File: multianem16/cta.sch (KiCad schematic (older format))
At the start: 243 parts, among them Q1 TIP41, Q10 TIP41, Q11 TIP41, Q12 TIP41, Q13 TIP41, Q14 TIP41, Q15 TIP41, Q16 TIP41, Q2 TIP41, Q3 TIP41, Q4 TIP41, Q5 TIP41, Q6 TIP41, Q7 TIP41, Q8 TIP41, Q9 TIP41, U1 LM324, U10 LM324, U11 LM324, U12 LM324, U13 LM324, U14 LM324, U15 LM324, U16 LM324, U2 LM324, U3 LM324, U4 LM324, U5 LM324, U6 LM324, U7 LM324, U8 LM324, U9 LM324

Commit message: Working on making the multinanem16 board use symmetric power input.
This way I can use more types of op-amps.
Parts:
- removed Cua1, Cua2, Cua3, Cua4, Cua5: 10u, Capacitor_THT:CP_Radial_D5.0mm_P2.50mm, symbol Device:CP
- removed JVIN1: Conn_01x02, TerminalBlock:TerminalBlock_bornier-2_P5.08mm, symbol Connector_Generic:Conn_01x02
- added Cua1, Cua2, Cua3, Cua4, Cua5: 100n, Capacitor_THT:C_Rect_L7.2mm_W3.5mm_P5.00mm_FKS2_FKP2_MKS2_MKP2, symbol Device:C
- added JVIN1: Conn_01x06, TerminalBlock:TerminalBlock_bornier-6_P5.08mm, symbol Connector_Generic:Conn_01x06
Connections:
- net GND: now also Cua1.2, Cua2.2, Cua3.2, Cua4.2, Cua5.2, JVIN1.3 (Pin_3), JVIN1.4 (Pin_4); no longer U1.11 (V-), U2.11 (V-), U3.11 (V-), U4.11 (V-), U5.11 (V-)
- net VCC: now also JVIN1.1 (Pin_1), JVIN1.2 (Pin_2)
- new net VEE: Cua1.1, Cua2.1, Cua3.1, Cua4.1, Cua5.1, JVIN1.5 (Pin_5), JVIN1.6 (Pin_6), U1.11 (V-), U2.11 (V-), U3.11 (V-), U4.11 (V-), U5.11 (V-)

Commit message: Working on adding symmetric power to the multianem16 board.
Almost done.
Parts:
- removed Cua10, Cua11, Cua12, Cua13, Cua14, Cua15, Cua16, Cua6, Cua7, Cua8, Cua9: 10u, Capacitor_THT:CP_Radial_D5.0mm_P2.50mm, symbol Device:CP
- added Cua10, Cua13, Cua14, Cua15, Cua16, Cua6, Cua7, Cua8, Cua9, Cub12, Cub17: 100n, Capacitor_THT:C_Rect_L7.2mm_W3.5mm_P5.00mm_FKS2_FKP2_MKS2_MKP2, symbol Device:C
- renumbered Cub12 to Cua12
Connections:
- net GND: now also JVIN1.5 (Pin_5), JVIN1.6 (Pin_6), Cua10.2, Cua13.2, Cua14.2, Cua15.2, Cua16.2, Cua6.2, Cua7.2, Cua8.2, Cua9.2, Cub12.2, Cub17.2; no longer JVIN1.3 (Pin_3), JVIN1.4 (Pin_4), U10.11 (V-), U11.11 (V-), U12.11 (V-), U13.11 (V-), U14.11 (V-), U15.11 (V-), U16.11 (V-), U6.11 (V-), U7.11 (V-), U8.11 (V-), U9.11 (V-)
- net VCC: now also Cub12.1; no longer Cua12.1
- net VEE: now also Cua12.1, JVIN1.3 (Pin_3), JVIN1.4 (Pin_4), U10.11 (V-), U11.11 (V-), U12.11 (V-), U13.11 (V-), U14.11 (V-), U15.11 (V-), U16.11 (V-), U6.11 (V-), U7.11 (V-), U8.11 (V-), U9.11 (V-), Cua10.1, Cua13.1, Cua14.1, Cua15.1, Cua16.1, Cua6.1, Cua7.1, Cua8.1, Cua9.1, Cub17.1; no longer JVIN1.5 (Pin_5), JVIN1.6 (Pin_6)
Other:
- moved on the sheet: Cua12

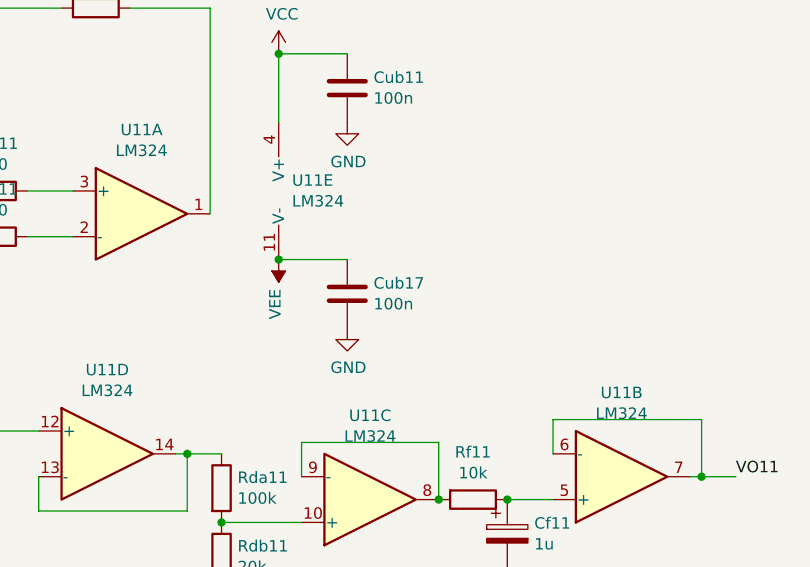
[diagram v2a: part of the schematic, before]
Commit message: Finnished adding Vee to the 16 anemometers board.
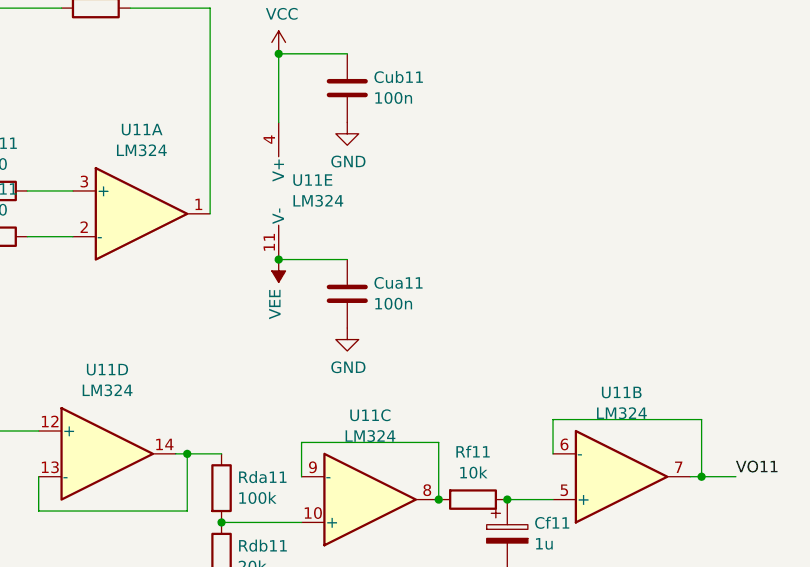
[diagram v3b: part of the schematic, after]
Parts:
- renumbered Cub17 to Cua11
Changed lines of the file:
@@
 EESchema Schematic File Version 4
-LIBS:cta-cache
 EELAYER 30 0
 EELAYER END
@@
 Connection ~ -3600 2900
 $Comp
-L Device:C Cub17
+L Device:C Cua11
 U 1 1 60D7259A
 P -3500 -650
-F 0 "Cub17" H -3385 -604 50  0000 L CNN
+F 0 "Cua11" H -3385 -604 50  0000 L CNN
 F 1 "100n" H -3385 -695 50  0000 L CNN
 F 2 "Capacitor_THT:C_Rect_L7.2mm_W3.5mm_P5.00mm_FKS2_FKP2_MKS2_MKP2" H -3462 -800 50  0001 C CNN

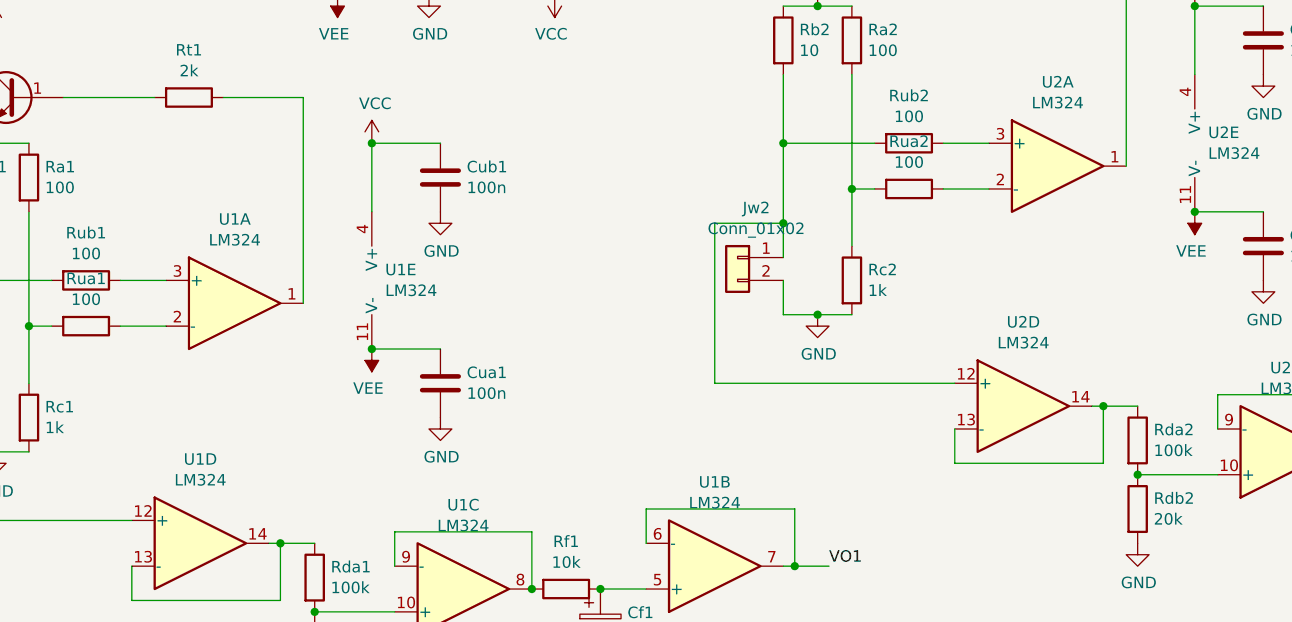
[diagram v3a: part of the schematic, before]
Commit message: Working on new circuit
Changed TerminalBlock footprint to pin header for thermistor probe.
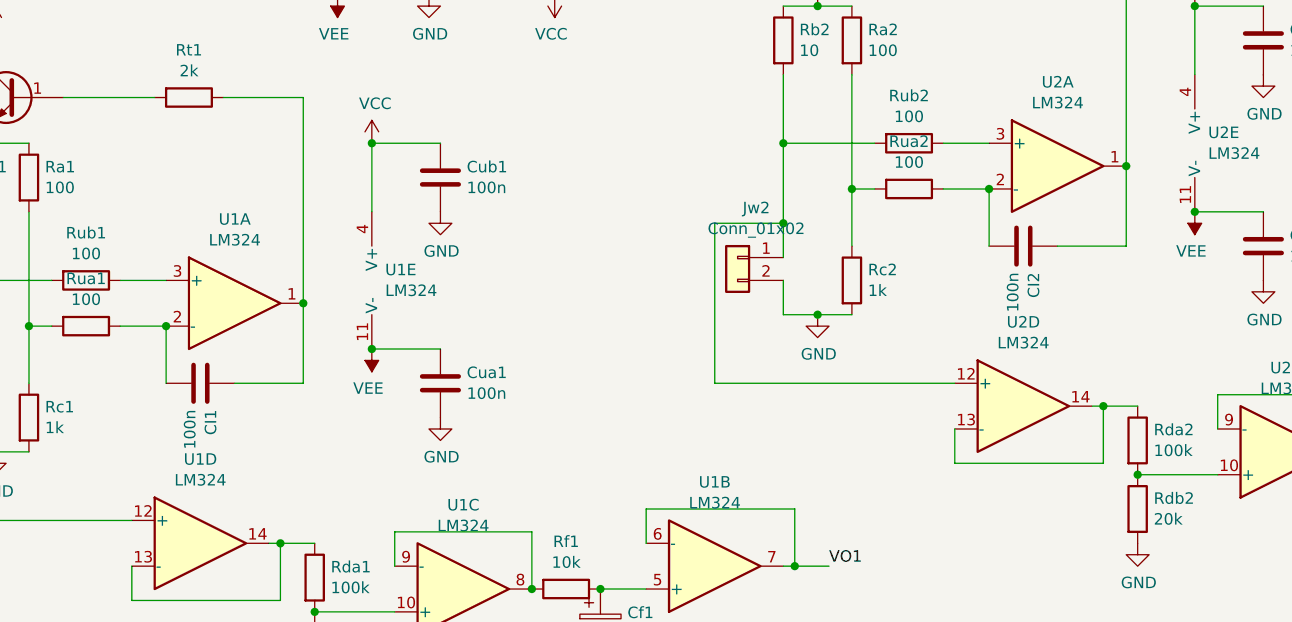
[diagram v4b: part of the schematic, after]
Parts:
- added CI1, CI2: 100n, Capacitor_THT:C_Rect_L7.2mm_W3.5mm_P5.00mm_FKS2_FKP2_MKS2_MKP2, symbol Device:C
- Jw1, Jw10, Jw11, Jw12, Jw13, Jw14, Jw15, Jw16, Jw2, Jw3, Jw4, Jw5, Jw6, Jw7, Jw8, Jw9: footprint TerminalBlock:TerminalBlock_bornier-2_P5.08mm -> Connector_PinHeader_2.54mm:PinHeader_1x02_P2.54mm_Vertical
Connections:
- net at Rt1.1, U1.1: now also CI1.1
- net at Rua1.1, U1.2 (-): now also CI1.2
- net at Rt2.1, U2.1: now also CI2.1
- net at Rua2.1, U2.2 (-): now also CI2.2
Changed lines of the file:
@@
 F 0 "Jw1" H 518 2867 50  0000 C CNN
 F 1 "Conn_01x02" H 518 2776 50  0000 C CNN
-F 2 "TerminalBlock:TerminalBlock_bornier-2_P5.08mm" H 600 2650 50  0001 C CNN
+F 2 "Connector_PinHeader_2.54mm:PinHeader_1x02_P2.54mm_Vertical" H 600 2650 50  0001 C CNN
 F 3 "~" H 600 2650 50  0001 C CNN
 	1    600  2650
@@
 F 0 "Jw2" H 4118 2267 50  0000 C CNN
 F 1 "Conn_01x02" H 4118 2176 50  0000 C CNN
-F 2 "TerminalBlock:TerminalBlock_bornier-2_P5.08mm" H 4200 2050 50  0001 C CNN
+F 2 "Connector_PinHeader_2.54mm:PinHeader_1x02_P2.54mm_Vertical" H 4200 2050 50  0001 C CNN
 F 3 "~" H 4200 2050 50  0001 C CNN
 	1    4200 2050
@@
 F 0 "Jw3" H 7668 1717 50  0000 C CNN
 F 1 "Conn_01x02" H 7668 1626 50  0000 C CNN
-F 2 "TerminalBlock:TerminalBlock_bornier-2_P5.08mm" H 7750 1500 50  0001 C CNN
+F 2 "Connector_PinHeader_2.54mm:PinHeader_1x02_P2.54mm_Vertical" H 7750 1500 50  0001 C CNN
 F 3 "~" H 7750 1500 50  0001 C CNN
 	1    7750 1500
@@
 F 0 "Jw4" H 11718 1217 50  0000 C CNN
 F 1 "Conn_01x02" H 11718 1126 50  0000 C CNN
-F 2 "TerminalBlock:TerminalBlock_bornier-2_P5.08mm" H 11800 1000 50  0001 C CNN
+F 2 "Connector_PinHeader_2.54mm:PinHeader_1x02_P2.54mm_Vertical" H 11800 1000 50  0001 C CNN
 F 3 "~" H 11800 1000 50  0001 C CNN
 	1    11800 1000
@@
 F 0 "Jw5" H 15868 817 50  0000 C CNN
 F 1 "Conn_01x02" H 15868 726 50  0000 C CNN
-F 2 "TerminalBlock:TerminalBlock_bornier-2_P5.08mm" H 15950 600 50  0001 C CNN
+F 2 "Connector_PinHeader_2.54mm:PinHeader_1x02_P2.54mm_Vertical" H 15950 600 50  0001 C CNN
 F 3 "~" H 15950 600 50  0001 C CNN
 	1    15950 600
@@
 F 0 "Jw6" H 16118 4017 50  0000 C CNN
 F 1 "Conn_01x02" H 16118 3926 50  0000 C CNN
-F 2 "TerminalBlock:TerminalBlock_bornier-2_P5.08mm" H 16200 3800 50  0001 C CNN
+F 2 "Connector_PinHeader_2.54mm:PinHeader_1x02_P2.54mm_Vertical" H 16200 3800 50  0001 C CNN
 F 3 "~" H 16200 3800 50  0001 C CNN
 	1    16200 3800
@@
 F 0 "Jw7" H 20168 417 50  0000 C CNN
 F 1 "Conn_01x02" H 20168 326 50  0000 C CNN
-F 2 "TerminalBlock:TerminalBlock_bornier-2_P5.08mm" H 20250 200 50  0001 C CNN
+F 2 "Connector_PinHeader_2.54mm:PinHeader_1x02_P2.54mm_Vertical" H 20250 200 50  0001 C CNN
 F 3 "~" H 20250 200 50  0001 C CNN
 	1    20250 200
@@
 F 0 "Jw8" H 19968 3417 50  0000 C CNN
 F 1 "Conn_01x02" H 19968 3326 50  0000 C CNN
-F 2 "TerminalBlock:TerminalBlock_bornier-2_P5.08mm" H 20050 3200 50  0001 C CNN
+F 2 "Connector_PinHeader_2.54mm:PinHeader_1x02_P2.54mm_Vertical" H 20050 3200 50  0001 C CNN
 F 3 "~" H 20050 3200 50  0001 C CNN
 	1    20050 3200
@@
 F 0 "Jw9" H -6082 6817 50  0000 C CNN
 F 1 "Conn_01x02" H -6082 6726 50  0000 C CNN
-F 2 "TerminalBlock:TerminalBlock_bornier-2_P5.08mm" H -6000 6600 50  0001 C CNN
+F 2 "Connector_PinHeader_2.54mm:PinHeader_1x02_P2.54mm_Vertical" H -6000 6600 50  0001 C CNN
 F 3 "~" H -6000 6600 50  0001 C CNN
 	1    -6000 6600
@@
 F 0 "Jw10" H -5682 3317 50  0000 C CNN
 F 1 "Conn_01x02" H -5682 3226 50  0000 C CNN
-F 2 "TerminalBlock:TerminalBlock_bornier-2_P5.08mm" H -5600 3100 50  0001 C CNN
+F 2 "Connector_PinHeader_2.54mm:PinHeader_1x02_P2.54mm_Vertical" H -5600 3100 50  0001 C CNN
 F 3 "~" H -5600 3100 50  0001 C CNN
 	1    -5600 3100
@@
 F 0 "Jw11" H -5882 -383 50  0000 C CNN
 F 1 "Conn_01x02" H -5882 -474 50  0000 C CNN
-F 2 "TerminalBlock:TerminalBlock_bornier-2_P5.08mm" H -5800 -600 50  0001 C CNN
+F 2 "Connector_PinHeader_2.54mm:PinHeader_1x02_P2.54mm_Vertical" H -5800 -600 50  0001 C CNN
 F 3 "~" H -5800 -600 50  0001 C CNN
 	1    -5800 -600
@@
 F 0 "Jw12" H -732 -1283 50  0000 C CNN
 F 1 "Conn_01x02" H -732 -1374 50  0000 C CNN
-F 2 "TerminalBlock:TerminalBlock_bornier-2_P5.08mm" H -650 -1500 50  0001 C CNN
+F 2 "Connector_PinHeader_2.54mm:PinHeader_1x02_P2.54mm_Vertical" H -650 -1500 50  0001 C CNN
 F 3 "~" H -650 -1500 50  0001 C CNN
 	1    -650 -1500
@@
 F 0 "Jw13" H 3718 -1483 50  0000 C CNN
 F 1 "Conn_01x02" H 3718 -1574 50  0000 C CNN
-F 2 "TerminalBlock:TerminalBlock_bornier-2_P5.08mm" H 3800 -1700 50  0001 C CNN
+F 2 "Connector_PinHeader_2.54mm:PinHeader_1x02_P2.54mm_Vertical" H 3800 -1700 50  0001 C CNN
 F 3 "~" H 3800 -1700 50  0001 C CNN
 	1    3800 -1700
@@
 F 0 "Jw14" H 8168 -2383 50  0000 C CNN
 F 1 "Conn_01x02" H 8168 -2474 50  0000 C CNN
-F 2 "TerminalBlock:TerminalBlock_bornier-2_P5.08mm" H 8250 -2600 50  0001 C CNN
+F 2 "Connector_PinHeader_2.54mm:PinHeader_1x02_P2.54mm_Vertical" H 8250 -2600 50  0001 C CNN
 F 3 "~" H 8250 -2600 50  0001 C CNN
 	1    8250 -2600
@@
 F 0 "Jw15" H 12718 -2433 50  0000 C CNN
 F 1 "Conn_01x02" H 12718 -2524 50  0000 C CNN
-F 2 "TerminalBlock:TerminalBlock_bornier-2_P5.08mm" H 12800 -2650 50  0001 C CNN
+F 2 "Connector_PinHeader_2.54mm:PinHeader_1x02_P2.54mm_Vertical" H 12800 -2650 50  0001 C CNN
 F 3 "~" H 12800 -2650 50  0001 C CNN
 	1    12800 -2650
@@
 F 0 "Jw16" H 17168 -2833 50  0000 C CNN
 F 1 "Conn_01x02" H 17168 -2924 50  0000 C CNN
-F 2 "TerminalBlock:TerminalBlock_bornier-2_P5.08mm" H 17250 -3050 50  0001 C CNN
+F 2 "Connector_PinHeader_2.54mm:PinHeader_1x02_P2.54mm_Vertical" H 17250 -3050 50  0001 C CNN
 F 3 "~" H 17250 -3050 50  0001 C CNN
 	1    17250 -3050
@@
 	19550 -3250 19250 -3250
 Connection ~ 19250 -3250
+$Comp
+L Device:C CI1
+U 1 1 608A539A
+P 1850 2600
+F 0 "CI1" H 1965 2646 50  0000 L CNN
+F 1 "100n" H 1965 2555 50  0000 L CNN
+F 2 "Capacitor_THT:C_Rect_L7.2mm_W3.5mm_P5.00mm_FKS2_FKP2_MKS2_MKP2" H 1888 2450 50  0001 C CNN
+F 3 "~" H 1850 2600 50  0001 C CNN
+	1    1850 2600
+	0    1    1    0
+$EndComp
+Wire Wire Line
+	1700 2600 1700 2350
+Connection ~ 1700 2350
+Wire Wire Line
+	2000 2600 2300 2600
+Wire Wire Line
+	2300 2600 2300 2250
+Connection ~ 2300 2250
+$Comp
+L Device:C CI2
+U 1 1 6098D750
+P 5450 2000
+F 0 "CI2" H 5565 2046 50  0000 L CNN
+F 1 "100n" H 5565 1955 50  0000 L CNN
+F 2 "Capacitor_THT:C_Rect_L7.2mm_W3.5mm_P5.00mm_FKS2_FKP2_MKS2_MKP2" H 5488 1850 50  0001 C CNN
+F 3 "~" H 5450 2000 50  0001 C CNN
+	1    5450 2000
+	0    1    1    0
+$EndComp
+Wire Wire Line
+	5300 2000 5300 1750
+Connection ~ 5300 1750
+Wire Wire Line
+	5600 2000 5900 2000
+Wire Wire Line
+	5900 2000 5900 1650
+Connection ~ 5900 1650
 $EndSCHEMATC

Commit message: The multianem16 board is almost ready: need to replace Ron by an diode
The problem is that with a resistor every single anemometer is coupled to the others. A diode (1n4148) should isolate them.

The board that I built was kind of poor. Too many flaws in the traces.
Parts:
- added CI10, CI11, CI12, CI13, CI14, CI15, CI16, CI3, CI4, CI5, CI6, CI7, CI8, CI9: 100n, Capacitor_THT:C_Rect_L7.2mm_W3.5mm_P5.00mm_FKS2_FKP2_MKS2_MKP2, symbol Device:C
- added Coo1: 10u, Capacitor_THT:CP_Radial_D5.0mm_P2.50mm, symbol Device:CP
- added D1: 1N4001, Diode_THT:D_DO-41_SOD81_P10.16mm_Horizontal, symbol Diode:1N4001
- added Qon1: 2N3906, Package_TO_SOT_THT:TO-92_Inline_Wide, symbol Transistor_BJT:2N3906
- added Ron1, Ron10, Ron11, Ron12, Ron13, Ron14, Ron15, Ron16, Ron2, Ron3, Ron4, Ron5, Ron6, Ron7, Ron8, Ron9: 100, Resistor_THT:R_Axial_DIN0207_L6.3mm_D2.5mm_P15.24mm_Horizontal, symbol Device:R
- added Roo1: 10, Resistor_THT:R_Axial_DIN0207_L6.3mm_D2.5mm_P10.16mm_Horizontal, symbol Device:R
- added Roo2: 22k, Resistor_THT:R_Axial_DIN0207_L6.3mm_D2.5mm_P10.16mm_Horizontal, symbol Device:R
- added Roo3: 4.7k, Resistor_THT:R_Axial_DIN0207_L6.3mm_D2.5mm_P10.16mm_Horizontal, symbol Device:R
- Cua1, Cua10, Cua11, Cua12, Cua13, Cua14, Cua15, Cua16, Cua2, Cua3, Cua4, Cua5, Cua6, Cua7, Cua8, Cua9, Cub1, Cub10, Cub11, Cub12, Cub13, Cub14, Cub15, Cub16, Cub2, Cub3, Cub4, Cub5, Cub6, Cub7, Cub8, Cub9: footprint Capacitor_THT:C_Rect_L7.2mm_W3.5mm_P5.00mm_FKS2_FKP2_MKS2_MKP2 -> Capacitor_THT:C_Disc_D5.0mm_W2.5mm_P2.50mm
- Rb1, Rb10, Rb11, Rb12, Rb13, Rb14, Rb15, Rb16, Rb2, Rb3, Rb4, Rb5, Rb6, Rb7, Rb8, Rb9: footprint Resistor_THT:R_Axial_Power_L20.0mm_W6.4mm_P22.40mm -> Resistor_THT:R_Axial_DIN0414_L11.9mm_D4.5mm_P15.24mm_Horizontal
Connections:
- net GND: now also Coo1.2, Roo3.2
- net VCC: now also D1.2 (A), Roo2.1, Roo3.1
- net at Q1.1 (B), Rt1.2: now also Ron1.1
- net at Q2.1 (B), Rt2.2: now also Ron2.1
- net at Rt3.1, U3.1: now also CI3.1
- net at Rua3.1, U3.2 (-): now also CI3.2
- net at Q3.1 (B), Rt3.2: now also Ron3.1
- net at Rt4.1, U4.1: now also CI4.1
- net at Rua4.1, U4.2 (-): now also CI4.2
- net at Q4.1 (B), Rt4.2: now also Ron4.1
- net at Rt5.1, U5.1: now also CI5.1
- net at Rua5.1, U5.2 (-): now also CI5.2
- net at Q5.1 (B), Rt5.2: now also Ron5.1
- net at Q6.1 (B), Rt6.2: now also Ron6.1
- net at Rt6.1, U6.1: now also CI6.1
- net at Rua6.1, U6.2 (-): now also CI6.2
- net at Q7.1 (B), Rt7.2: now also Ron7.1
- net at Rt7.1, U7.1: now also CI7.1
- net at Rua7.1, U7.2 (-): now also CI7.2
- net at Q8.1 (B), Rt8.2: now also Ron8.1
- net at Rt8.1, U8.1: now also CI8.1
- net at Rua8.1, U8.2 (-): now also CI8.2
- net at Q9.1 (B), Rt9.2: now also Ron9.1
- net at Rt9.1, U9.1: now also CI9.1
- net at Rua9.1, U9.2 (-): now also CI9.2
- net at Q10.1 (B), Rt10.2: now also Ron10.1
- net at Rt10.1, U10.1: now also CI10.1
- net at Rua10.1, U10.2 (-): now also CI10.2
- net at Q11.1 (B), Rt11.2: now also Ron11.1
- net at Rt11.1, U11.1: now also CI11.1
- net at Rua11.1, U11.2 (-): now also CI11.2
- net at Q12.1 (B), Rt12.2: now also Ron12.1
- net at Rt12.1, U12.1: now also CI12.1
- net at Rua12.1, U12.2 (-): now also CI12.2
- net at Q13.1 (B), Rt13.2: now also Ron13.1
- net at Rt13.1, U13.1: now also CI13.1
- net at Rua13.1, U13.2 (-): now also CI13.2
- net at Q14.1 (B), Rt14.2: now also Ron14.1
- net at Rt14.1, U14.1: now also CI14.1
- net at Rua14.1, U14.2 (-): now also CI14.2
- net at Q15.1 (B), Rt15.2: now also Ron15.1
- net at Rt15.1, U15.1: now also CI15.1
- net at Rua15.1, U15.2 (-): now also CI15.2
- net at Q16.1 (B), Rt16.2: now also Ron16.1
- net at Rt16.1, U16.1: now also CI16.1
- net at Rua16.1, U16.2 (-): now also CI16.2
- new net: D1.1 (K), Qon1.1 (E)
- new net: Coo1.1, Roo1.1, Roo2.2
- new net: Qon1.2 (B), Roo1.2
- new net VON1: Qon1.3 (C), Ron1.2, Ron10.2, Ron11.2, Ron12.2, Ron13.2, Ron14.2, Ron15.2, Ron16.2, Ron2.2, Ron3.2, Ron4.2, Ron5.2, Ron6.2, Ron7.2, Ron8.2, Ron9.2

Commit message: Replaced the Ron? resistors by Don? capacitors
I tested the original board and it appeared to be working. Let's try this for real!
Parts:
- removed Ron1, Ron10, Ron11, Ron12, Ron13, Ron14, Ron15, Ron16, Ron2, Ron3, Ron4, Ron5, Ron6, Ron7, Ron8, Ron9: 100, Resistor_THT:R_Axial_DIN0207_L6.3mm_D2.5mm_P15.24mm_Horizontal, symbol Device:R
- added Don1, Don10, Don11, Don12, Don13, Don14, Don15, Don16, Don2, Don3, Don4, Don5, Don6, Don7, Don8, Don9: 1N4148, Diode_THT:D_DO-35_SOD27_P7.62mm_Horizontal, symbol Diode:1N4148
- Rua1, Rua10, Rua11, Rua12, Rua13, Rua14, Rua15, Rua16, Rua2, Rua3, Rua4, Rua5, Rua6, Rua7, Rua8, Rua9, Rub1, Rub10, Rub11, Rub12, Rub13, Rub14, Rub15, Rub16, Rub2, Rub3, Rub4, Rub5, Rub6, Rub7, Rub8, Rub9: value 100 -> 10k
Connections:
- net VON1: now also Don1.2 (A), Don10.2 (A), Don11.2 (A), Don12.2 (A), Don13.2 (A), Don14.2 (A), Don15.2 (A), Don16.2 (A), Don2.2 (A), Don3.2 (A), Don4.2 (A), Don5.2 (A), Don6.2 (A), Don7.2 (A), Don8.2 (A), Don9.2 (A)
- net at Q1.1 (B), Rt1.2: now also Don1.1 (K)
- net at Q2.1 (B), Rt2.2: now also Don2.1 (K)
- net at Q3.1 (B), Rt3.2: now also Don3.1 (K)
- net at Q4.1 (B), Rt4.2: now also Don4.1 (K)
- net at Q5.1 (B), Rt5.2: now also Don5.1 (K)
- net at Q6.1 (B), Rt6.2: now also Don6.1 (K)
- net at Q7.1 (B), Rt7.2: now also Don7.1 (K)
- net at Q8.1 (B), Rt8.2: now also Don8.1 (K)
- net at Q9.1 (B), Rt9.2: now also Don9.1 (K)
- net at Q10.1 (B), Rt10.2: now also Don10.1 (K)
- net at Q11.1 (B), Rt11.2: now also Don11.1 (K)
- net at Q12.1 (B), Rt12.2: now also Don12.1 (K)
- net at Q13.1 (B), Rt13.2: now also Don13.1 (K)
- net at Q14.1 (B), Rt14.2: now also Don14.1 (K)
- net at Q15.1 (B), Rt15.2: now also Don15.1 (K)
- net at Q16.1 (B), Rt16.2: now also Don16.1 (K)
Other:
- moved on the sheet: Cua6, Cub6, Jw8, U6B, U6E
